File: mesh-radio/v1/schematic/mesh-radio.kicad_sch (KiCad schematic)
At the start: 0 parts

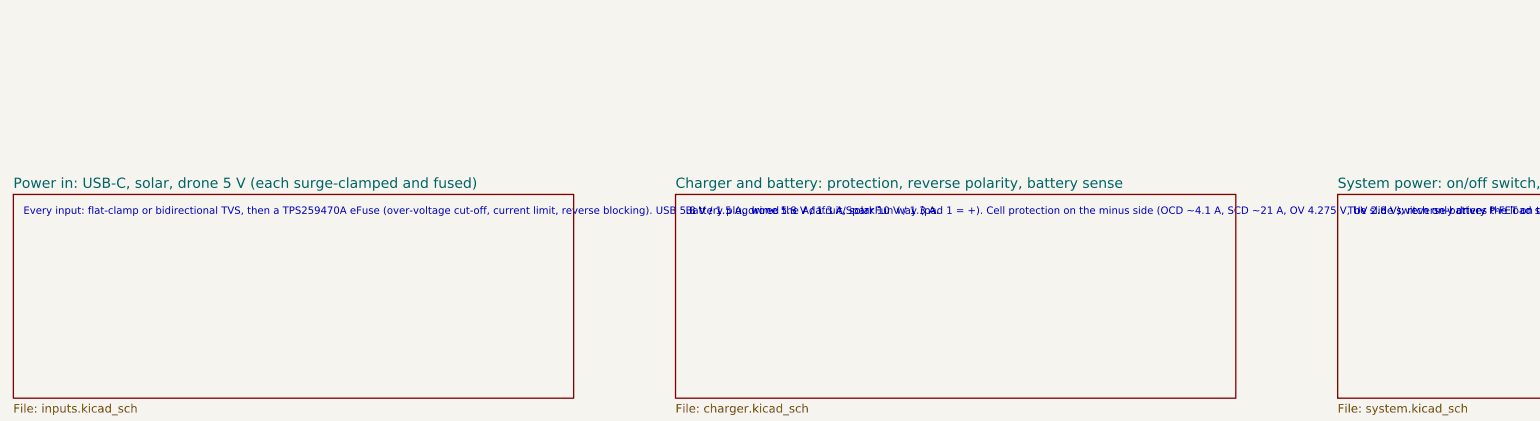
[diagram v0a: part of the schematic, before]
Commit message: Mesh Radio v1: fix every design-review finding, add the part audit
An independent review of the schematic found two critical and nine further
issues; all are fixed in src/circuit.py:
- reverse-battery FET gate now returns to the cell's own minus terminal, so
  a backwards cell stays isolated even while USB/solar/drone power the board
- solar and drone inputs: reverse-blocking Schottky + 22 V flat-clamp TVS
  (the 15 V TVS would have failed on a 12 V panel); 4.7 V clamp on every
  eFuse EN/UVLO pin so 20 V on an input stays inside its rating
- ideal diode (LM66100) holds VSYS on the cell when a 3 W burst trips the
  charger's 3.0 V battery disconnect
- charge LED moved to STAT2 (charging), USB cut-off lowered to 5.4 V,
  charger /CE on a GPIO for firmware temperature control, -40 C TCXO,
  power mux on only with the amplifier, header VSYS pin removed
- firmware ceilings documented: SX1262 +20 dBm, amplifier 3.6 V by default

docs/part-audit.md: all 125 lines checked at DigiKey and LCSC (genuine
LCSC numbers, DigiKey numbers, second sources for out-of-stock lines);
parts cost about $76 at 10 boards, $58 at 100.

Schematic regenerated: ERC 0 violations, netlist equals circuit.py.

Co-Authored-By: Claude Opus 5.5 <noreply@anthropic.com>
Claude-Session: https://claude.ai/code/session_015TBB2ThqxHSgA8MkFosmn9
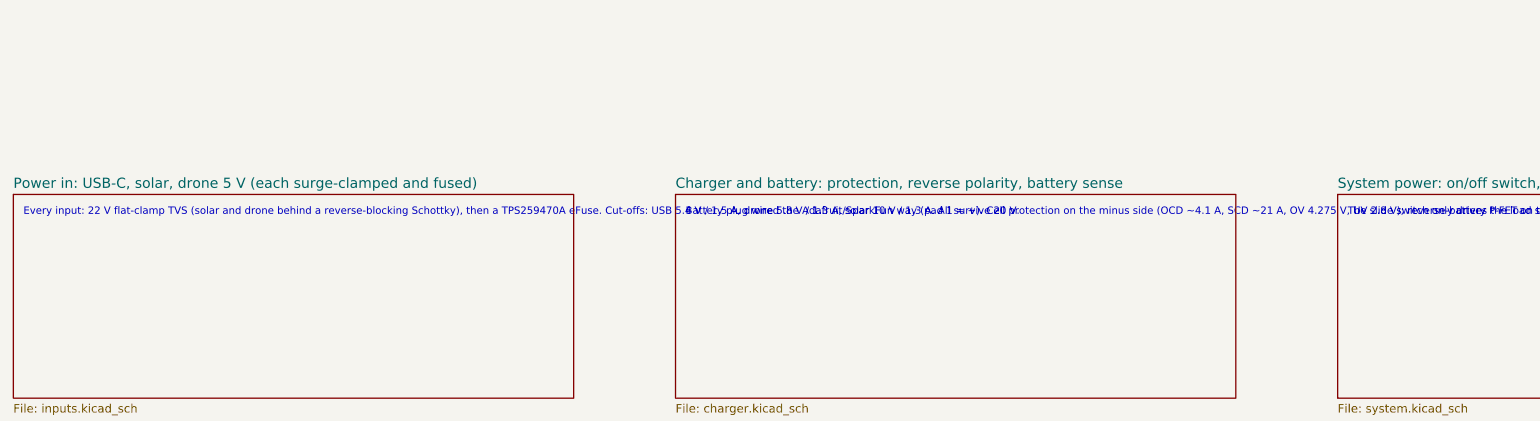
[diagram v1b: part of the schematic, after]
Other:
- note added: "Every input: 22 V flat-clamp TVS (solar and drone behind a reverse-blocking Schottky), then a TPS259470A eFuse. Cut-offs: USB 5.4 V / 1.5 A, drone 5.8 V / 1.3 A, solar 10 V / 1.3 A. All survive 20 V."
- note removed: "Every input: flat-clamp or bidirectional TVS, then a TPS259470A eFuse (over-voltage cut-off, current limit, reverse blocking). USB 5.8 V / 1.5 A, drone 5.8 V / 1.3 A, solar 10 V / 1.3 A."
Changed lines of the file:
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@@
 		)
 	)
-	(text "Every input: flat-clamp or bidirectional TVS, then a TPS259470A eFuse (over-voltage cut-off, current limit, reverse blocking). USB 5.8 V / 1.5 A, drone 5.8 V / 1.3 A, solar 10 V / 1.3 A."
+	(text "Every input: 22 V flat-clamp TVS (solar and drone behind a reverse-blocking Schottky), then a TPS259470A eFuse. Cut-offs: USB 5.4 V / 1.5 A, drone 5.8 V / 1.3 A, solar 10 V / 1.3 A. All survive 20 V."
 		(exclude_from_sim no)
 		(at 21.82 62.96 0)

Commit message: Mesh radio v1: power-path and firmware rework in progress (snapshot)
Co-Authored-By: Claude Opus 5.5 <noreply@anthropic.com>
Claude-Session: https://claude.ai/code/session_015TBB2ThqxHSgA8MkFosmn9
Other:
- note added: "Amplifier runs from the battery through a power mux (battery first down to 2.6 V; firmware selects charger SYS when no cell is fitted), then a TPS63810 buck-boost (I2C 0x75): 2.7 V for 1 W, 4.0 V for 3 W."
- note added: "Battery plug wired the Adafruit/SparkFun way (pad 1 = +). Cell protection on the minus side (OCD ~5.8 A, SCD ~29 A, OV 4.275 V, UV 2.8 V); reverse-battery P-FET on the plus side, on only when the cell is the right way round. Charge 300 mA. Current-limited cell-to-SYS bypass."
- note added: "The slide switch drives only enables (3.3 V buck, cell bypass); charging works with the board off."
- note added: "USB: 22 V flat-clamp TVS, a 4.7 uF + 1 R snubber and a TPS259470A eFuse (cut-off 5.4 V, 1.5 A). Solar and drone: 33 V TVS and a 60 V MAX17608 (cut-off 10 V, 0.71 A, blocks -60 V and reverse current)."
- note removed: "Amplifier runs from the battery through a power mux (charger SYS only when no battery), then a TPS63810 buck-boost set over I2C (0x75): ~2.7 V for 1 W, up to 4.0 V for 3 W."
- note removed: "Battery plug wired the Adafruit/SparkFun way (pad 1 = +). Cell protection on the minus side (OCD ~4.1 A, SCD ~21 A, OV 4.275 V, UV 2.8 V); reverse-battery P-FET on the plus side."
- note removed: "Every input: 22 V flat-clamp TVS (solar and drone behind a reverse-blocking Schottky), then a TPS259470A eFuse. Cut-offs: USB 5.4 V / 1.5 A, drone 5.8 V / 1.3 A, solar 10 V / 1.3 A. All survive 20 V."
- note removed: "The slide switch only drives the load switch enable; charging works with the board switched off."
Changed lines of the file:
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@@
 		)
 	)
-	(text "Every input: 22 V flat-clamp TVS (solar and drone behind a reverse-blocking Schottky), then a TPS259470A eFuse. Cut-offs: USB 5.4 V / 1.5 A, drone 5.8 V / 1.3 A, solar 10 V / 1.3 A. All survive 20 V."
+	(text "USB: 22 V flat-clamp TVS, a 4.7 uF + 1 R snubber and a TPS259470A eFuse (cut-off 5.4 V, 1.5 A). Solar and drone: 33 V TVS and a 60 V MAX17608 (cut-off 10 V, 0.71 A, blocks -60 V and reverse current)."
 		(exclude_from_sim no)
 		(at 21.82 62.96 0)
@@
 		)
 	)
-	(text "Battery plug wired the Adafruit/SparkFun way (pad 1 = +). Cell protection on the minus side (OCD ~4.1 A, SCD ~21 A, OV 4.275 V, UV 2.8 V); reverse-battery P-FET on the plus side."
+	(text "Battery plug wired the Adafruit/SparkFun way (pad 1 = +). Cell protection on the minus side (OCD ~5.8 A, SCD ~29 A, OV 4.275 V, UV 2.8 V); reverse-battery P-FET on the plus side, on only when the cell is the right way round. Charge 300 mA. Current-limited cell-to-SYS bypass."
 		(exclude_from_sim no)
 		(at 120.88 62.96 0)
@@
 		)
 	)
-	(text "The slide switch only drives the load switch enable; charging works with the board switched off."
+	(text "The slide switch drives only enables (3.3 V buck, cell bypass); charging works with the board off."
 		(exclude_from_sim no)
 		(at 219.94 62.96 0)
@@
 		)
 	)
-	(text "Amplifier runs from the battery through a power mux (charger SYS only when no battery), then a TPS63810 buck-boost set over I2C (0x75): ~2.7 V for 1 W, up to 4.0 V for 3 W."
+	(text "Amplifier runs from the battery through a power mux (battery first down to 2.6 V; firmware selects charger SYS when no cell is fitted), then a TPS63810 buck-boost (I2C 0x75): 2.7 V for 1 W, 4.0 V for 3 W."
 		(exclude_from_sim no)
 		(at 219.94 113.76 0)
